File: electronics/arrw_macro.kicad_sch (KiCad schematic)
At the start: 23 parts, among them J7 Conn_01x05_Female, J8 Conn_01x05_Male, SW59 SW_SPST, SW60 SW_SPST, SW61 SW_SPST, SW62 SW_SPST, SW63 SW_SPST, SW64 SW_SPST, SW65 SW_SPST, SW66 SW_SPST, SW67 SW_SPST, SW68 SW_SPST, U4 PCA9675PW

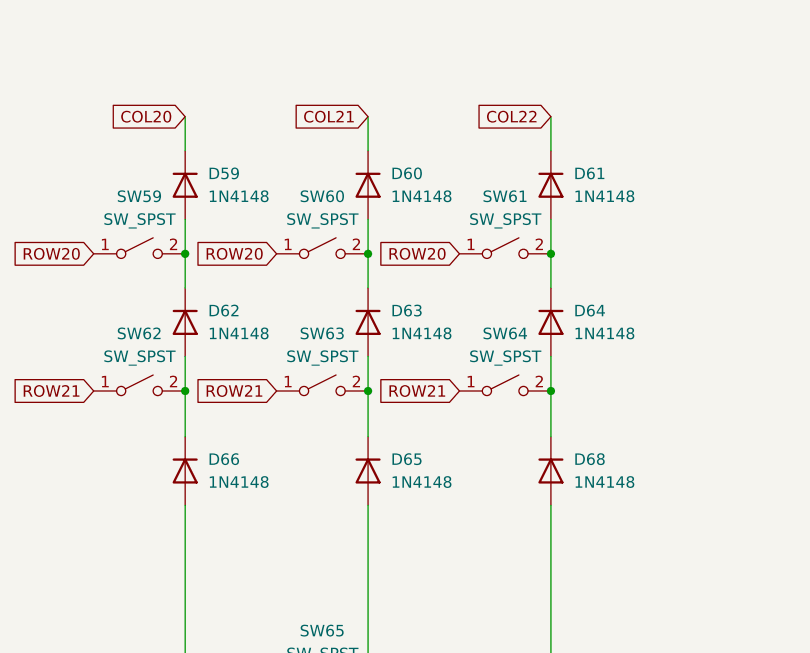
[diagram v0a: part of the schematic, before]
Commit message: update diode libraries
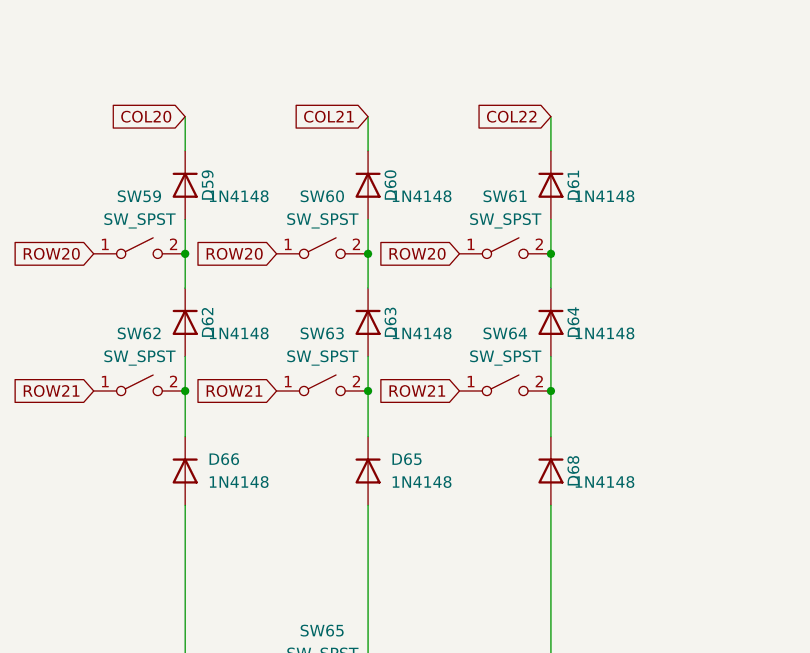
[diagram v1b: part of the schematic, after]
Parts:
- D59, D60, D61, D62, D63, D64, D65, D66, D67, D68: footprint Diode_SMD:D_SOD-123 -> 1N4148:1N4148; symbol Diode:1N4148W -> 1N4148:1N4148

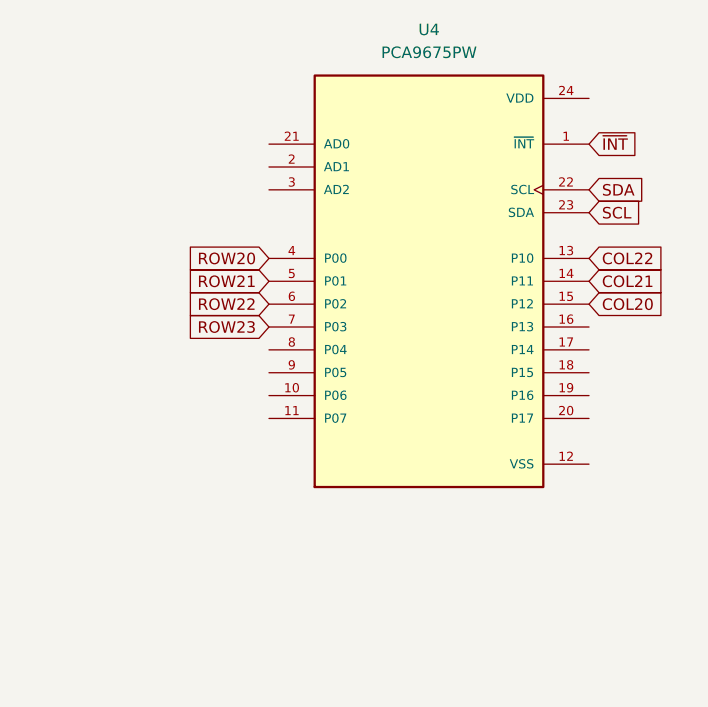
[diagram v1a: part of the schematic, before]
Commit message: add power and i2c addressing
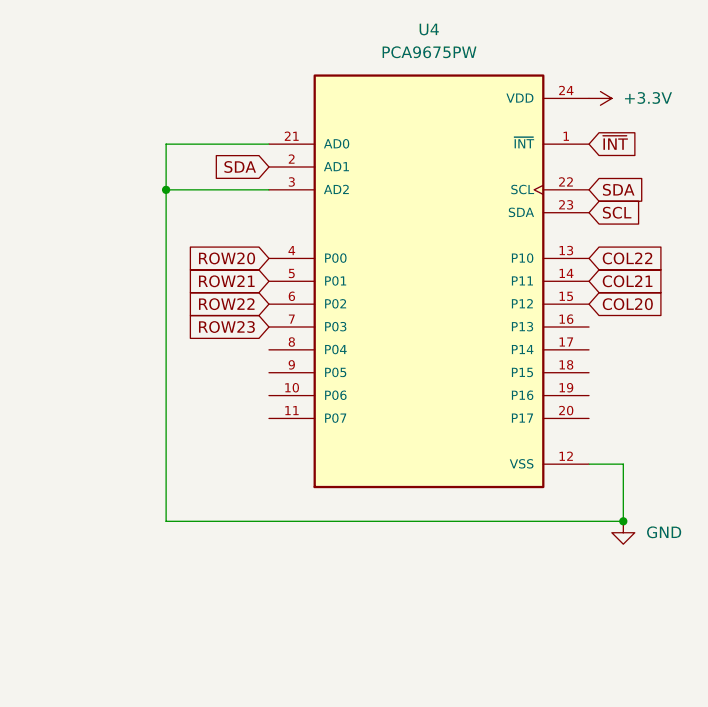
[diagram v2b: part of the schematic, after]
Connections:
- net +3V3: now also U4.24 (VDD)
- net GND: now also U4.12 (VSS), U4.21 (AD0), U4.3 (AD2)
- net SDA: now also U4.2 (AD1)
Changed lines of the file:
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@@
     (company "OSHMount Tech")
   )
+  (junction (at 177.8 46.99) (diameter 0) (color 0 0 0 0)
+  )
   (junction (at 93.98 106.68) (diameter 0) (color 0 0 0 0)
   )
@@
   (junction (at 114.3 106.68) (diameter 0) (color 0 0 0 0)
   )
+  (junction (at 228.6 83.82) (diameter 0) (color 0 0 0 0)
+  )
   (wire (pts (xy 114.3 118.11) (xy 114.3 121.92))
     (stroke (width 0) (type default) (color 0 0 0 0))
@@
     (stroke (width 0) (type default) (color 0 0 0 0))
   )
+  (wire (pts (xy 177.8 46.99) (xy 177.8 83.82))
+    (stroke (width 0) (type default) (color 0 0 0 0))
+  )
   (wire (pts (xy 114.3 91.44) (xy 114.3 95.25))
     (stroke (width 0) (type default) (color 0 0 0 0))
@@
     (stroke (width 0) (type default) (color 0 0 0 0))
   )
+  (wire (pts (xy 228.6 83.82) (xy 228.6 77.47))
+    (stroke (width 0) (type default) (color 0 0 0 0))
+  )
   (wire (pts (xy 93.98 118.11) (xy 93.98 121.92))
     (stroke (width 0) (type default) (color 0 0 0 0))
@@
     (stroke (width 0) (type default) (color 0 0 0 0))
   )
+  (wire (pts (xy 228.6 77.47) (xy 224.79 77.47))
+    (stroke (width 0) (type default) (color 0 0 0 0))
+  )
   (wire (pts (xy 93.98 134.62) (xy 93.98 154.94))
     (stroke (width 0) (type default) (color 0 0 0 0))
   )
+  (wire (pts (xy 177.8 46.99) (xy 189.23 46.99))
+    (stroke (width 0) (type default) (color 0 0 0 0))
+  )
+  (wire (pts (xy 177.8 83.82) (xy 228.6 83.82))
+    (stroke (width 0) (type default) (color 0 0 0 0))
+  )
   (wire (pts (xy 191.77 114.3) (xy 190.5 114.3))
     (stroke (width 0) (type default) (color 0 0 0 0))
@@
     (stroke (width 0) (type default) (color 0 0 0 0))
   )
+  (wire (pts (xy 189.23 41.91) (xy 177.8 41.91))
+    (stroke (width 0) (type default) (color 0 0 0 0))
+  )
   (wire (pts (xy 73.66 91.44) (xy 73.66 95.25))
     (stroke (width 0) (type default) (color 0 0 0 0))
@@
     (stroke (width 0) (type default) (color 0 0 0 0))
   )
+  (wire (pts (xy 177.8 41.91) (xy 177.8 46.99))
+    (stroke (width 0) (type default) (color 0 0 0 0))
+  )
   (wire (pts (xy 93.98 102.87) (xy 93.98 106.68))
     (stroke (width 0) (type default) (color 0 0 0 0))
@@
     (property "Intersheet References" "${INTERSHEET_REFS}" (id 0) (at 228.836 121.9994 0)
       (effects (font (size 1.27 1.27)) (justify left) hide)
+    )
+  )
+  (global_label "SDA" (shape input) (at 189.23 44.45 180) (fields_autoplaced)
+    (effects (font (size 1.27 1.27)) (justify right))
+    (property "Intersheet References" "${INTERSHEET_REFS}" (id 0) (at 183.2488 44.3706 0)
+      (effects (font (size 1.27 1.27)) (justify right) hide)
     )
   )
@@
       (effects (font (size 1.27 1.27)) hide)
     )
+    (pin "1")
+  )
+  (symbol (lib_id "power:GND") (at 228.6 83.82 0) (unit 1)
+    (in_bom yes) (on_board yes) (fields_autoplaced)
+    (property "Reference" "#PWR?" (id 0) (at 228.6 90.17 0)
+      (effects (font (size 1.27 1.27)) hide)
+    )
+    (property "Value" "GND" (id 1) (at 231.14 85.0899 0)
+      (effects (font (size 1.27 1.27)) (justify left))
+    )
+    (property "Footprint" "" (id 2) (at 228.6 83.82 0)
+      (effects (font (size 1.27 1.27)) hide)
+    )
+    (property "Datasheet" "" (id 3) (at 228.6 83.82 0)
+      (effects (font (size 1.27 1.27)) hide)
+    )
+    (pin "1")
+  )
+  (symbol (lib_id "power:+3.3V") (at 224.79 36.83 270) (unit 1)
+    (in_bom yes) (on_board yes) (fields_autoplaced)
+    (property "Reference" "#PWR?" (id 0) (at 220.98 36.83 0)
+      (effects (font (size 1.27 1.27)) hide)
+    )
+    (property "Value" "+3.3V" (id 1) (at 228.6 36.8299 90)
+      (effects (font (size 1.27 1.27)) (justify left))
+    )
+    (property "Footprint" "" (id 2) (at 224.79 36.83 0)
+      (effects (font (size 1.27 1.27)) hide)
+    )
+    (property "Datasheet" "" (id 3) (at 224.79 36.83 0)
+      (effects (font (size 1.27 1.27)) hide)
+    )
